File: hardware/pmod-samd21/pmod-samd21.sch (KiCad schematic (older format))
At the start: 18 parts, among them J1 PMOD-2x6-MALE, J2 PMOD-2x6-FEMALE, Q1 2N7002PW, U1 ATSAMD21G-A, Y1 32.768kHz

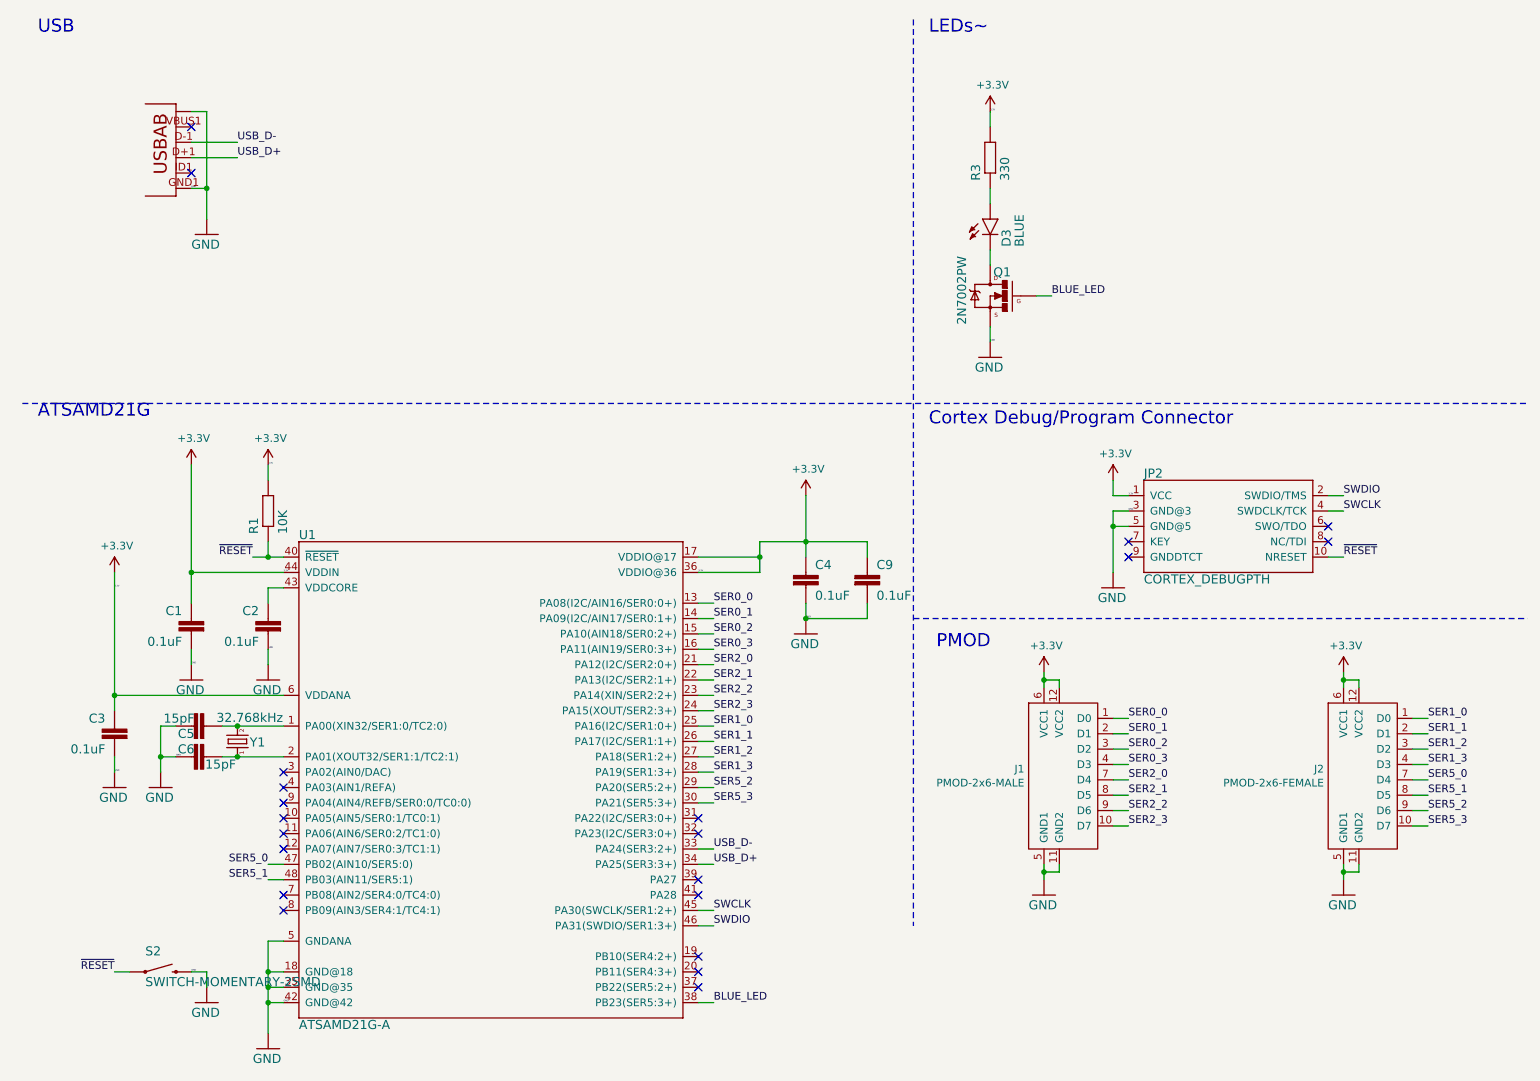
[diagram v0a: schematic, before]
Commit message: First pass at routing of samd21 pmod, power yet to be done
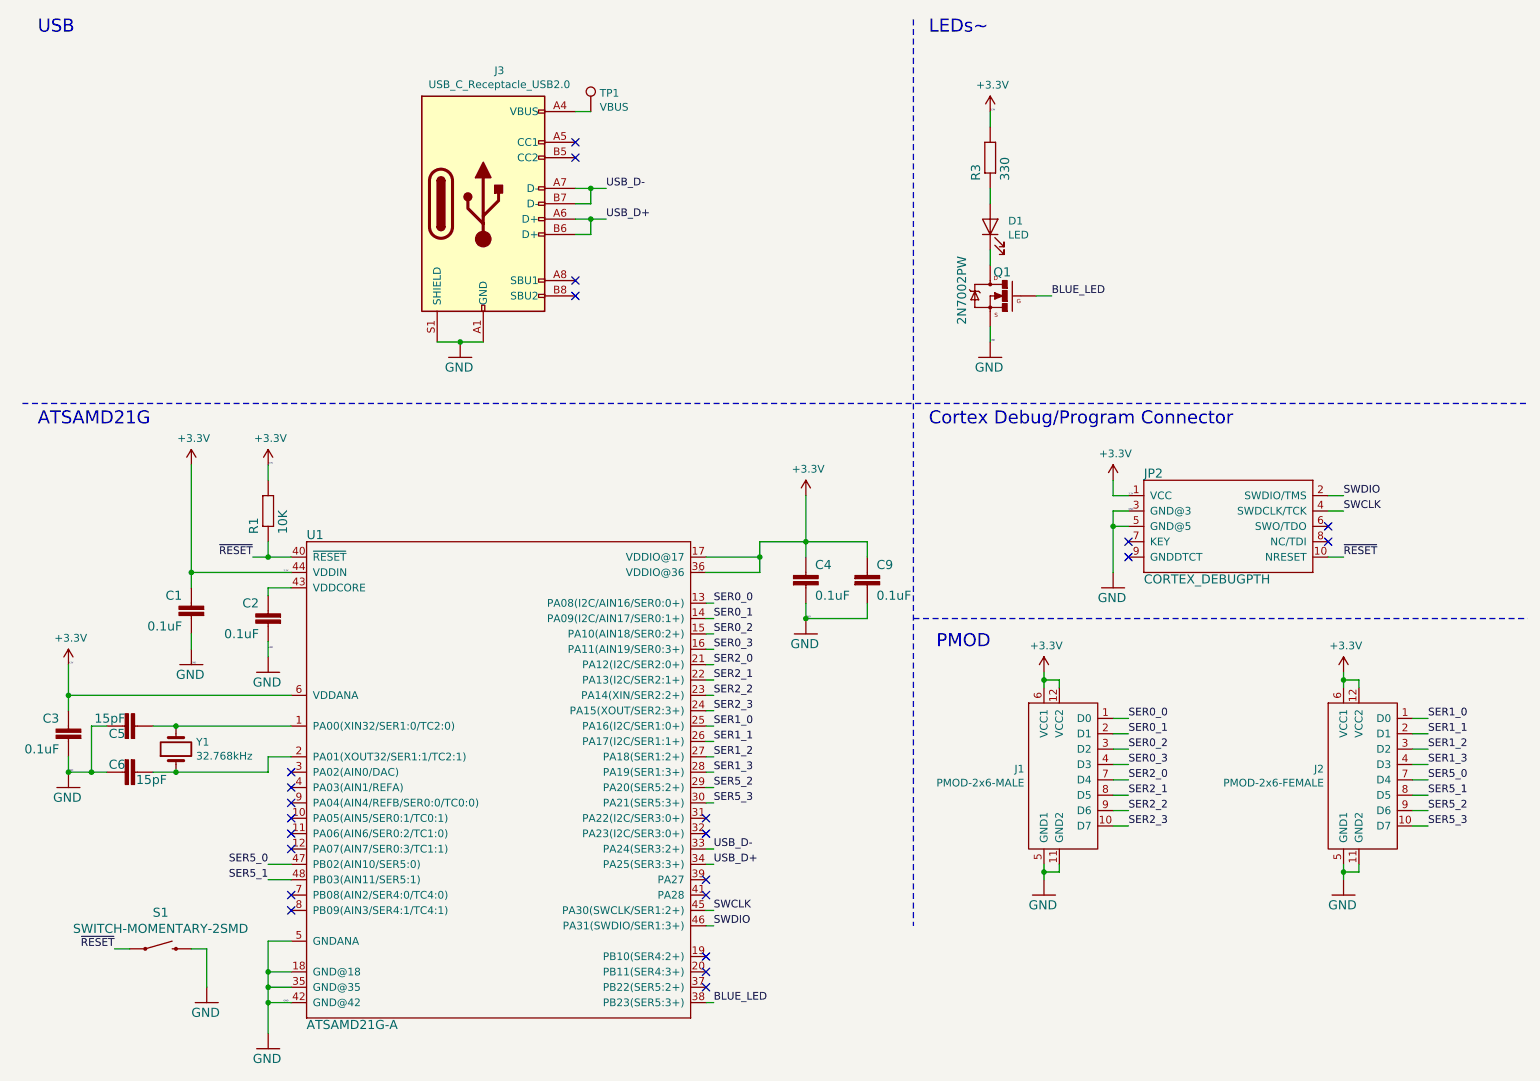
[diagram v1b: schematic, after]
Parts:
- removed D3: BLUE, pmod-samd21:LED-0603, symbol pmod-samd21-eagle-import:LED-BLUE0603
- removed JP1: USB-ABCONN-11794, pmod-samd21:USB-AB-MICRO-SMD_V03, symbol pmod-samd21-eagle-import:USB-ABCONN-11794
- removed S2: SWITCH-MOMENTARY-2SMD, pmod-samd21:TACTILE-SWITCH-SMD, symbol pmod-samd21-eagle-import:SWITCH-MOMENTARY-2SMD
- removed Y1: 32.768kHz, pmod-samd21:CRYSTAL-SMD-3.2X1.5MM, symbol pmod-samd21-eagle-import:CRYSTAL3.2X1.5MM
- added D1: LED, LEDs:LED_0402, symbol Device:LED
- added J3: USB_C_Receptacle_USB2.0, tom-connectors:USB_C_Receptacle_GT-USB-7010, symbol Connector:USB_C_Receptacle_USB2.0
- added S1: SWITCH-MOMENTARY-2SMD, tom-mechanical:SW_SPST_SMD_2PIN_3.5x6.0, symbol pmod-samd21-eagle-import:SWITCH-MOMENTARY-2SMD
- added TP1: VBUS, Measurement_Points:Measurement_Point_Round-SMD-Pad_Small, symbol Connector:TestPoint
- added Y1: 32.768kHz, Crystals:Crystal_SMD_3215-2pin_3.2x1.5mm, symbol Device:Crystal
- C1, C2, C3, C4, C5, C6, C9: footprint pmod-samd21:0402-CAP -> Capacitors_SMD:C_0402
- J2: footprint (none) -> tom-connectors:2X6_SMD_RA_SOCKET
- JP2: footprint pmod-samd21:2X5-PTH-1.27MM -> tom-connectors:CONN_1.27_2x5
- Q1: footprint pmod-samd21:SOT323 -> TO_SOT_Packages_SMD:SOT-323_SC-70_Handsoldering
- R1, R3: footprint pmod-samd21:R0402 -> Resistors_SMD:R_0402
- U1: footprint pmod-samd21:TQFP-48 -> tom-semiconductors:QFP50P900X900X120-48N
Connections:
- net GND: now also J3.A1 (GND), J3.A12 (GND), J3.B1 (GND), J3.B12 (GND), J3.S1 (SHIELD); no longer C1.2
- net USB_D+: now also J3.A6 (D+), J3.B6 (D+)
- net USB_D-: now also J3.A7 (D-), J3.B7 (D-)
- net ~RESET: now also S1.1
- net at C6.1, U1.2 (PA01(XOUT32/SER1:1/TC2:1)): now also Y1.1
- net at C5.2, U1.1 (PA00(XIN32/SER1:0/TC2:0)): now also Y1.2
- net at R3.1: now also D1.2 (A)
- net at Q1.3 (D): now also D1.1 (K)
- new net VBUS: J3.A4 (VBUS), J3.A9 (VBUS), J3.B4 (VBUS), J3.B9 (VBUS), TP1.1
- no-connect marks 21 -> 23
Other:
- moved on the sheet: C1, C2, C3, C5, C6, U1

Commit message: pmod-samd21 - added missing usb C resistors - generated gerbers relative to aux origin
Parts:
- added R2, R4: 5.1k, Resistors_SMD:R_0402, symbol pmod-samd21-eagle-import:R-EU_R0402
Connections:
- net at J3.A5 (CC1): now also R4.2
- net at J3.B5 (CC2): now also R2.2
- new net: R2.1, R4.1
- no-connect marks 23 -> 21
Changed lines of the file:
@@
 NoConn ~ 4500 2500
 NoConn ~ 4500 2400
-NoConn ~ 4500 1600
-NoConn ~ 4500 1500
 $Comp
 L Device:Crystal Y1
@@
 Wire Wire Line
 	1900 5600 2500 5600
+$Comp
+L pmod-samd21-eagle-import:R-EU_R0402 R2
+U 1 0 5C0A44EE
+P 5300 1800
+F 0 "R2" H 5150 1859 59  0000 L BNN
+F 1 "5.1k" H 5150 1670 59  0000 L BNN
+F 2 "Resistors_SMD:R_0402" H 5300 1800 50  0001 C CNN
+F 3 "" H 5300 1800 50  0001 C CNN
+	1    5300 1800
+	0    -1   -1   0
+$EndComp
+$Comp
+L pmod-samd21-eagle-import:R-EU_R0402 R4
+U 1 0 5C0A4650
+P 5600 1800
+F 0 "R4" H 5450 1859 59  0000 L BNN
+F 1 "5.1k" H 5450 1670 59  0000 L BNN
+F 2 "Resistors_SMD:R_0402" H 5600 1800 50  0001 C CNN
+F 3 "" H 5600 1800 50  0001 C CNN
+	1    5600 1800
+	0    -1   -1   0
+$EndComp
+$Comp
+L pmod-samd21-eagle-import:GND #GND05
+U 1 0 5C0A4784
+P 5450 2150
+F 0 "#GND05" H 5450 2150 50  0001 C CNN
+F 1 "GND" H 5350 2050 59  0000 L BNN
+F 2 "" H 5450 2150 50  0001 C CNN
+F 3 "" H 5450 2150 50  0001 C CNN
+	1    5450 2150
+	1    0    0    -1
+$EndComp
+Wire Wire Line
+	5300 2000 5300 2050
+Wire Wire Line
+	5300 2050 5450 2050
+Wire Wire Line
+	5450 2050 5600 2050
+Wire Wire Line
+	5600 2050 5600 2000
+Connection ~ 5450 2050
+Wire Wire Line
+	5300 1600 4500 1600
+Wire Wire Line
+	4500 1500 5600 1500
+Wire Wire Line
+	5600 1500 5600 1600
 $EndSCHEMATC
